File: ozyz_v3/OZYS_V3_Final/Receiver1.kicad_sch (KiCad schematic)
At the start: 13 parts, among them Q7 AO3401A, Q8 2N7002

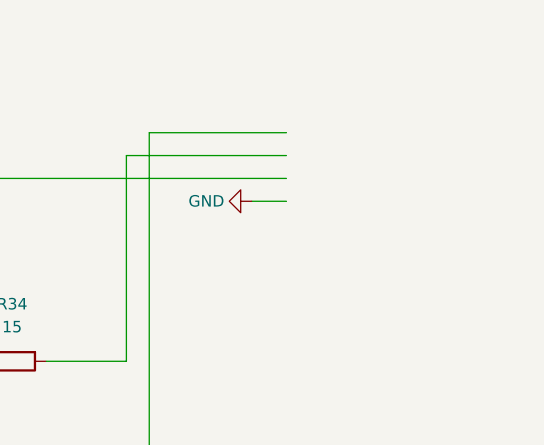
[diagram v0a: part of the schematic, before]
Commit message: OZYS and EPSILON schematics updated.
OZYS
- New 3.5 PJ-320A-4P DIP
- Fixed TPS Regulator Connections
- Fixed STM32 Connections
- Added Associated .ioc for stm32 pin config
- Loading Capacitance of LSE based off  an5093 STM datasheet
EPSILON
- same 3.5 as OZYS
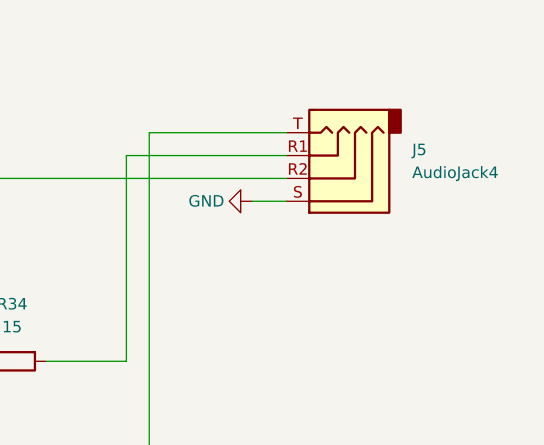
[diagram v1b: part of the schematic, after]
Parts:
- added J5: AudioJack4, Rocketry_Easyeda:AUDIO-TH_PJ-320A-4P-DIP, symbol Connector_Audio:AudioJack4
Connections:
- net GND: now also J5.S
- net at R22.2: now also J5.T
- net at Q7.2 (S), R25.1, R27.2: now also J5.R2
- net at R34.2: now also J5.R1
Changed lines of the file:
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@@
+	)
+	(symbol
+		(lib_id "Connector_Audio:AudioJack4")
+		(at 199.39 68.58 180)
+		(unit 1)
+		(exclude_from_sim no)
+		(in_bom yes)
+		(on_board yes)
+		(dnp no)
+		(fields_autoplaced yes)
+		(property "Reference" "J5"
+			(at 208.28 65.4049 0)
+			(effects
+				(font
+					(size 1.27 1.27)
+				)
+				(justify right)
+			)
+		)
+		(property "Value" "AudioJack4"
+			(at 208.28 67.9449 0)
+			(effects
+				(font
+					(size 1.27 1.27)
+				)
+				(justify right)
+			)
+		)
+		(property "Footprint" "Rocketry_Easyeda:AUDIO-TH_PJ-320A-4P-DIP"
+			(at 199.39 68.58 0)
+			(effects
+				(font
+					(size 1.27 1.27)
+				)
+				(hide yes)
+			)
+		)
+		(property "Datasheet" "~"
+			(at 199.39 68.58 0)
+			(effects
+				(font
+					(size 1.27 1.27)
+				)
+				(hide yes)
+			)
+		)
+		(property "Description" "Audio Jack, 4 Poles (TRRS)"
+			(at 199.39 68.58 0)
+			(effects
+				(font
+					(size 1.27 1.27)
+				)
+				(hide yes)
+			)
+		)
+		(pin "T"
+		)
+		(pin "S"
+		)
+		(pin "R1"
+		)
+		(pin "R2"
+		)
+		(instances
+			(project ""
+				(path "/2ecddb92-e766-42eb-adbc-b6d17a65e8ea/55853f5b-0992-495b-b96a-8743589b5403"
+					(reference "J5")
+					(unit 1)
+				)
+				(path "/2ecddb92-e766-42eb-adbc-b6d17a65e8ea/6e4545c6-9e5c-4e6b-94f2-451b2f16f4ae"
+					(reference "J4")
+					(unit 1)
+				)
+				(path "/2ecddb92-e766-42eb-adbc-b6d17a65e8ea/92ea14e4-7796-41b2-9af7-4cb5ffd88b52"
+					(reference "J3")
+					(unit 1)
+				)
+				(path "/2ecddb92-e766-42eb-adbc-b6d17a65e8ea/d66c3d32-3008-485f-b8d3-7e1a6a0b22a4"
+					(reference "J6")
+					(unit 1)
+				)
+			)
+		)
 	)
 	(symbol
